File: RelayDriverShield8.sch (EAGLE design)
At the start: 74 parts, among them IC1 MCP23017SO, J1 Analog, J2 POWER, J3 Digital_0_7, J4 M100.1, J5 ICSPPTH, J7 PWR SELECT, Q1 2N7002, Q2 2N7002, Q3 2N7002, Q4 2N7002, Q5 2N7002, Q6 2N7002, Q7 2N7002, Q8 2N7002

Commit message: Updated SKU and schematic PDF
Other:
- note added: "SKU: RELAY8"
- note removed: "SKU: SH-RELAY8"
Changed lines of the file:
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@@
 <text x="134.62" y="20.32" size="3.048" layer="94">Freetronics 8-Channel Relay Driver Shield</text>
 <text x="167.64" y="14.478" size="1.778" layer="94">V2.0 (2014-06-02)</text>
-<text x="134.62" y="14.478" size="1.778" layer="94">SKU: SH-RELAY8</text>
+<text x="134.62" y="14.478" size="1.778" layer="94">SKU: RELAY8</text>
 <text x="8.382" y="121.92" size="2.54" layer="94" ratio="12" rot="R90">Arduino Headers</text>
 <text x="137.16" y="62.738" size="1.778" layer="94">Power / Reset</text>

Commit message: Added solder jumper to link IOREF and 5V
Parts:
- added SJ4: (no value), freetronics-jon:SJN
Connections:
- net 5V: now also SJ4.2
- net IOREF: now also SJ4.1
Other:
- note added: "5V/IOREF Link"
- note added: "V2.0 (2014-06-06)"
- note removed: "V2.0 (2014-06-02)"
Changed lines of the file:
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@@
 <part name="J2" library="freetronics" deviceset="M08" device="" value="POWER"/>
 <part name="12V7" library="SparkFun" deviceset="VCC" device=""/>
+<part name="SJ4" library="freetronics-jon" deviceset="SJ" device="N"/>
+<part name="12V1" library="SparkFun" deviceset="VCC" device=""/>
 </parts>
 <sheets>
@@
 <wire x1="43.18" y1="38.1" x2="43.18" y2="5.08" width="0.4064" layer="97" style="longdash"/>
 <text x="134.62" y="20.32" size="3.048" layer="94">Freetronics 8-Channel Relay Driver Shield</text>
-<text x="167.64" y="14.478" size="1.778" layer="94">V2.0 (2014-06-02)</text>
+<text x="167.64" y="14.478" size="1.778" layer="94">V2.0 (2014-06-06)</text>
 <text x="134.62" y="14.478" size="1.778" layer="94">SKU: RELAY8</text>
 <text x="8.382" y="121.92" size="2.54" layer="94" ratio="12" rot="R90">Arduino Headers</text>
@@
 <text x="119.38" y="100.838" size="1.778" layer="94">ICSP
 Passthrough</text>
+<text x="116.84" y="123.698" size="1.778" layer="94">5V/IOREF Link</text>
 </plain>
 <instances>
@@
 <attribute name="VALUE" x="37.084" y="163.576" size="1.778" layer="96"/>
 </instance>
+<instance part="SJ4" gate="1" x="127" y="114.3"/>
+<instance part="12V1" gate="1" x="114.3" y="116.84" smashed="yes">
+<attribute name="VALUE" x="113.284" y="120.396" size="1.778" layer="96"/>
+</instance>
 </instances>
 <busses>
@@
 <pinref part="J2" gate="G$1" pin="2"/>
 </segment>
+<segment>
+<pinref part="SJ4" gate="1" pin="1"/>
+<wire x1="121.92" y1="114.3" x2="114.3" y2="114.3" width="0.1524" layer="91"/>
+<wire x1="114.3" y1="114.3" x2="114.3" y2="116.84" width="0.1524" layer="91"/>
+<label x="114.3" y="114.3" size="1.778" layer="95"/>
+<pinref part="12V1" gate="1" pin="VCC"/>
+</segment>
 </net>
 <net name="R3_SDA" class="0">
@@
 <pinref part="J2" gate="G$1" pin="5"/>
 </segment>
-</net>
+<segment>
+<pinref part="SJ4" gate="1" pin="2"/>
+<wire x1="132.08" y1="114.3" x2="139.7" y2="114.3" width="0.1524" layer="91"/>
+<label x="134.62" y="114.3" size="1.778" layer="95"/>
+</segment>
+</net>

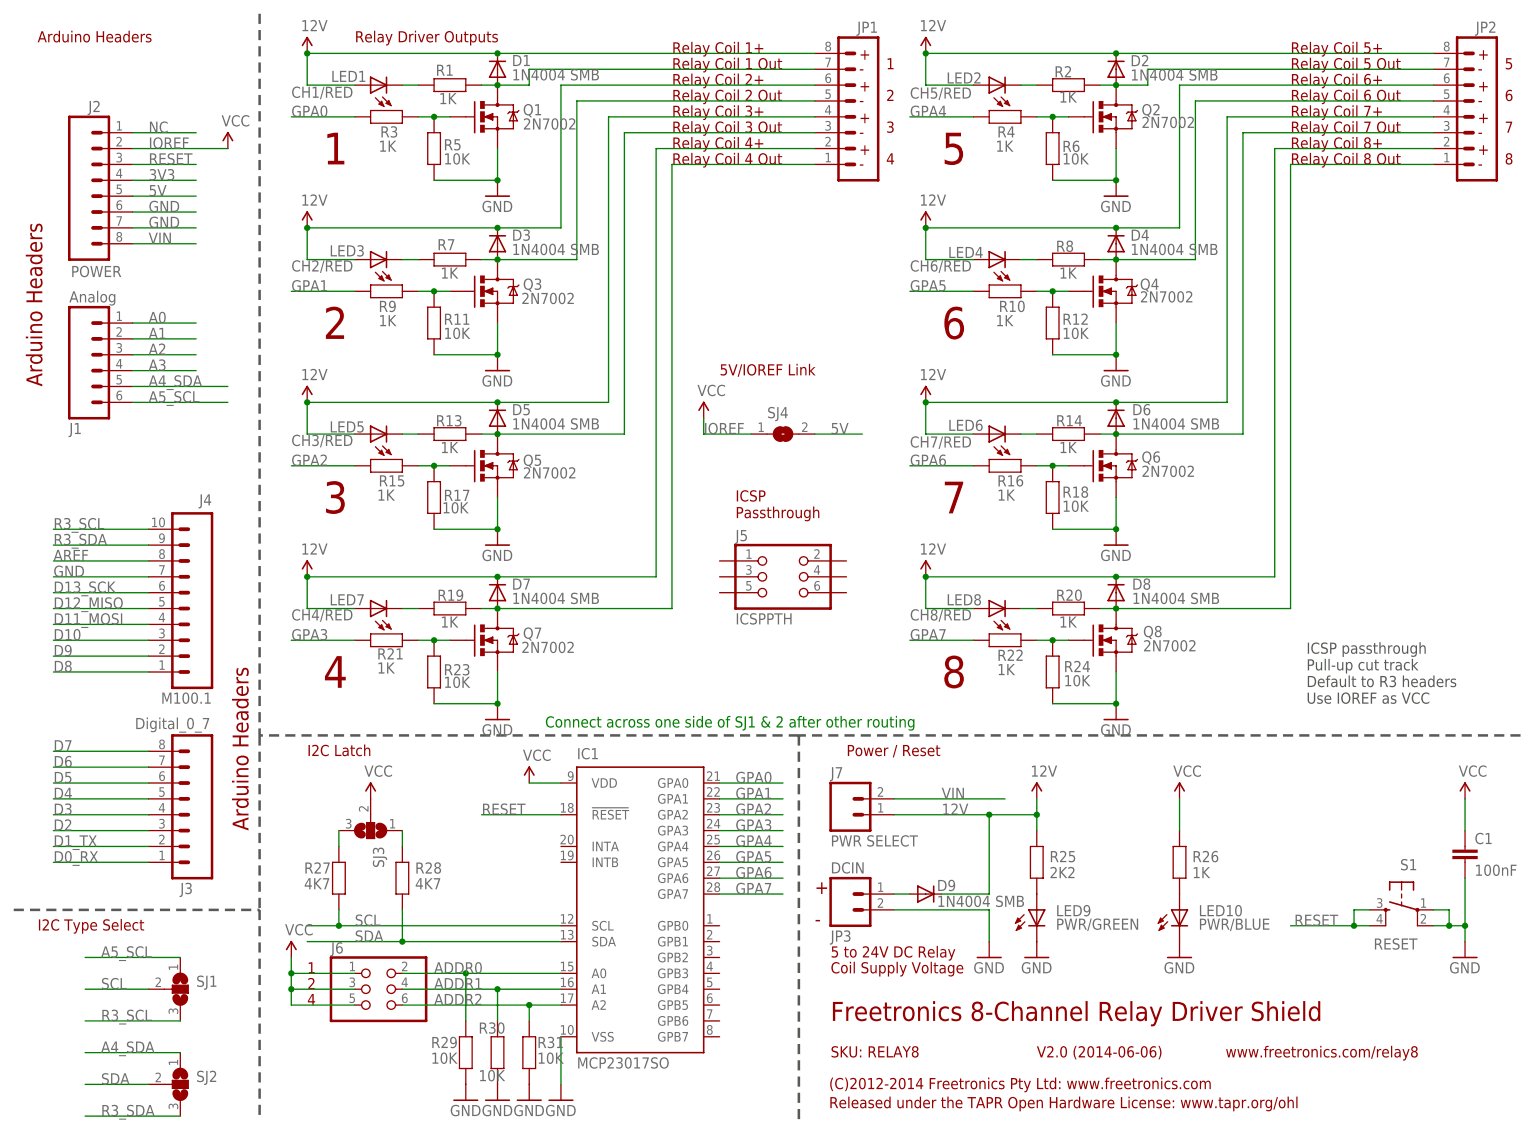
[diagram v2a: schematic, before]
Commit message: Replaced parts using SuperHouse library to add 3D models
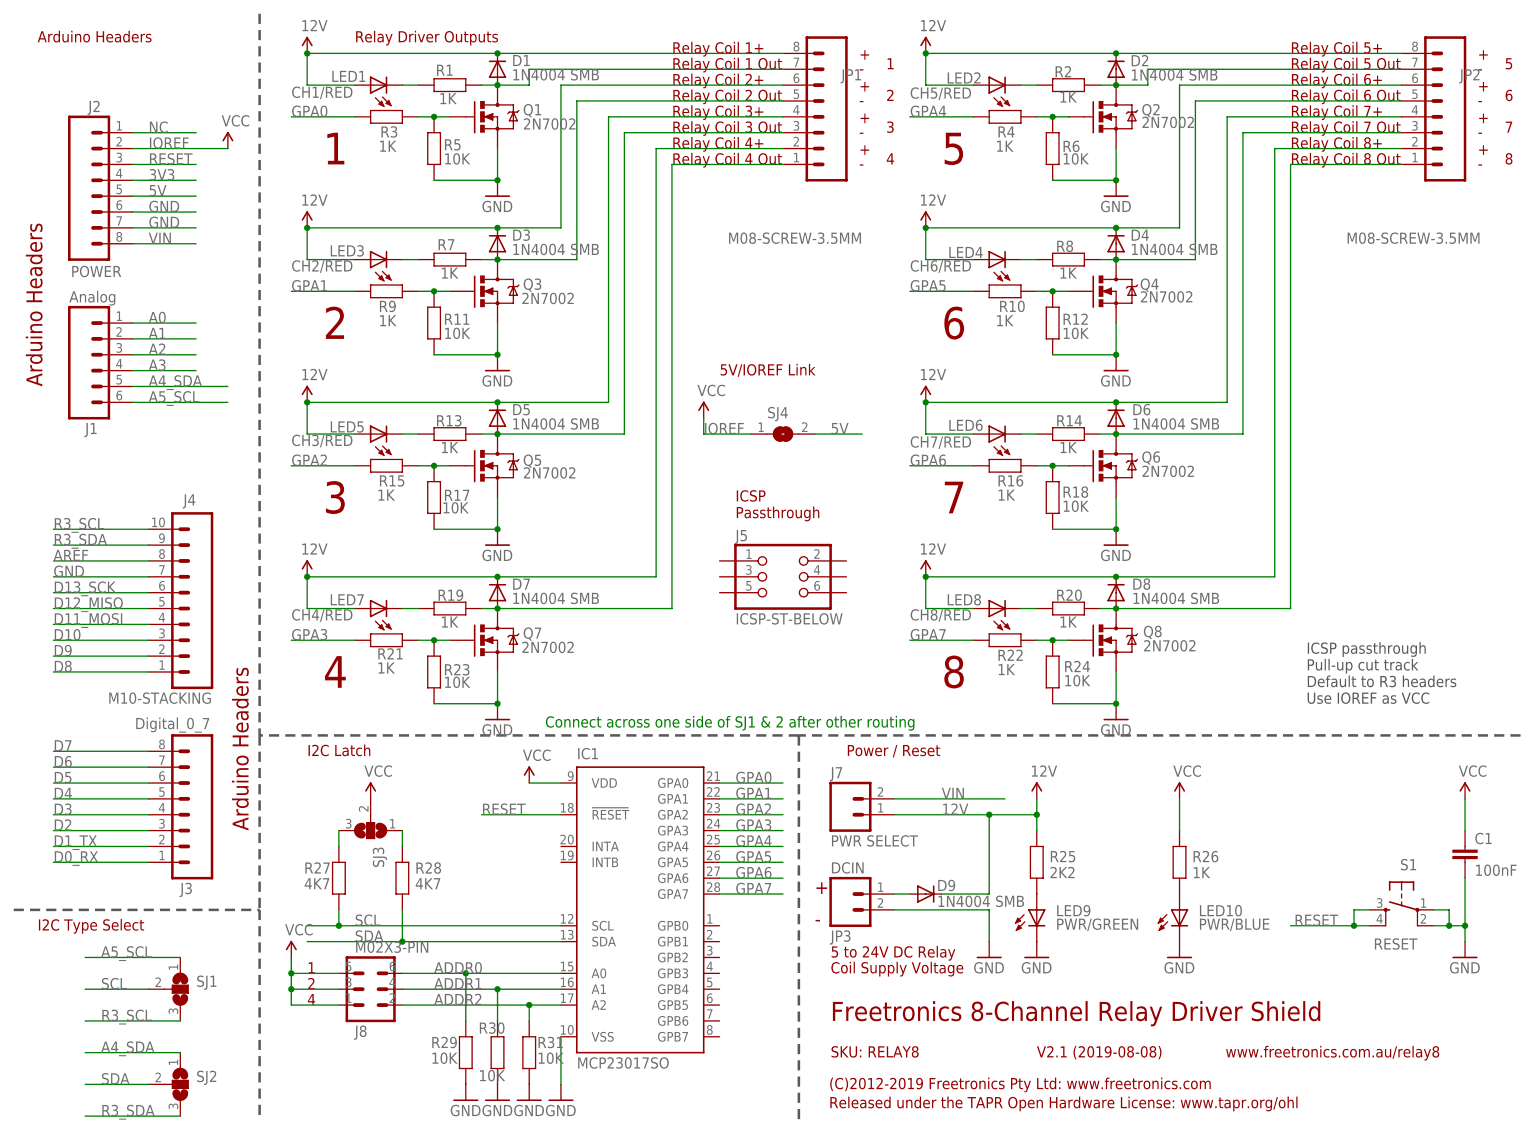
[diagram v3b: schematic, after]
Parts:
- removed J6: (no value), freetronics-master-v1.1:PINHD-2X3
- added J8: M02X3-PIN, SuperHouse-Connectors:M02X3-PIN
- C1: device freetronics-original:CAP0603 -> SuperHouse-DiscreteSemi:CAP0603
- D1, D2, D3, D4, D5, D6, D7, D8, D9: device freetronics-master-v1.1:DIODESMB -> SuperHouse-DiscreteSemi:DIODESMA
- IC1: device microchip:MCP23017SO -> SuperHouse-ICs:MCP23017SO
- J1: device freetronics:M06SIP -> SuperHouse-Connectors:M06-STACKING
- J2, J3: device freetronics:M08 -> SuperHouse-Connectors:M08-STACKING
- J4: value M100.1 -> M10-STACKING; device freetronics-original:M100.1 -> SuperHouse-Connectors:M10-STACKING
- J5: value ICSPPTH -> ICSP-ST-BELOW; device freetronics-jon:ICSPPTH -> SuperHouse-Connectors:ICSP-ST-BELOW
- J7: device SparkFun:M02PTH -> SuperHouse-Connectors:M02-PIN
- JP1, JP2: value (none) -> M08-SCREW-3.5MM; device freetronics-master-v1:M08 -> SuperHouse-Connectors:M08-SCREW-3.5MM
- JP3: device freetronics-master-v1.1:M023.5MM -> SuperHouse-Connectors:M02-SCREW-3.5MM
- LED1, LED10, LED2, LED3, LED4, LED5, LED6, LED7, LED8, LED9: device freetronics-master-v1:LED0603 -> SuperHouse-LEDs:LED0603
- Q1, Q2, Q3, Q4, Q5, Q6, Q7, Q8: device freetronics-master-v1:MOSFET-NCHANNELSMD -> SuperHouse-DiscreteSemi:MOSFET-NCHANNEL-233
- R1, R10, R11, R12, R13, R14, R15, R16, R17, R18, R19, R2, R20, R21, R22, R23, R24, R25, R26, R27, R28, R29, R3, R30, R31, R4, R5, R6, R7, R8, R9: device freetronics-master-v1:RESISTOR0603 -> SuperHouse-DiscreteSemi:RESISTOR0603
- S1: device freetronics-original:TAC_SWITCHSMD -> SuperHouse-Switches:TAC_SWITCH-SMT-6
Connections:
- net ADDR0: now also J8.6; no longer J6.2
- net ADDR1: now also J8.4; no longer J6.4
- net ADDR2: now also J8.2; no longer J6.6
- net IOREF: now also J8.1, J8.3, J8.5; no longer J6.1, J6.3, J6.5
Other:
- note added: "(C)2012-2019 Freetronics Pty Ltd: www.freetronics.com"
- note added: "V2.1 (2019-08-08)"
- note added: "www.freetronics.com.au/relay8"
- note removed: "(C)2012-2014 Freetronics Pty Ltd: www.freetronics.com"
- note removed: "V2.0 (2014-06-06)"
- note removed: "www.freetronics.com/relay8"
- moved on the sheet: JP1, JP2
